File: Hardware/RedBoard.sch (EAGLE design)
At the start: 65 parts, among them IC3 LM1117, J1 POWER_JACKOVERPASTE_REDBOARD_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, J2 ICSP, Q1 ZXMP6A13FTA, Q2 2N7002PW, U1 FT231XS, U2 MIC5205, U3 ATMEGA328, Y1 16MHz

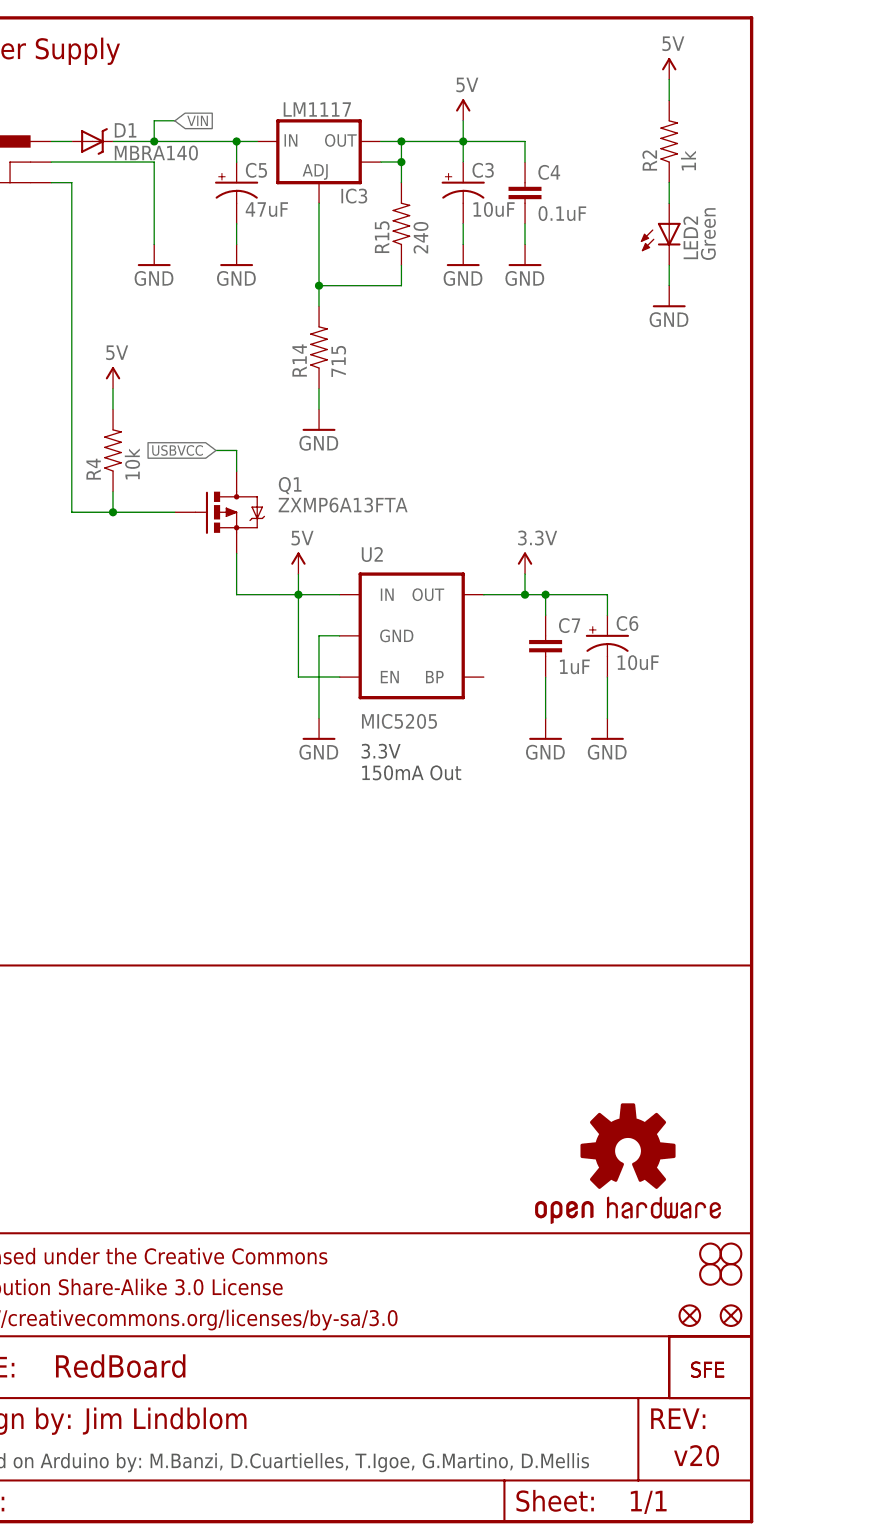
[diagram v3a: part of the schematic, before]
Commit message: Moved C1 cap around silk. Moved some top silk.
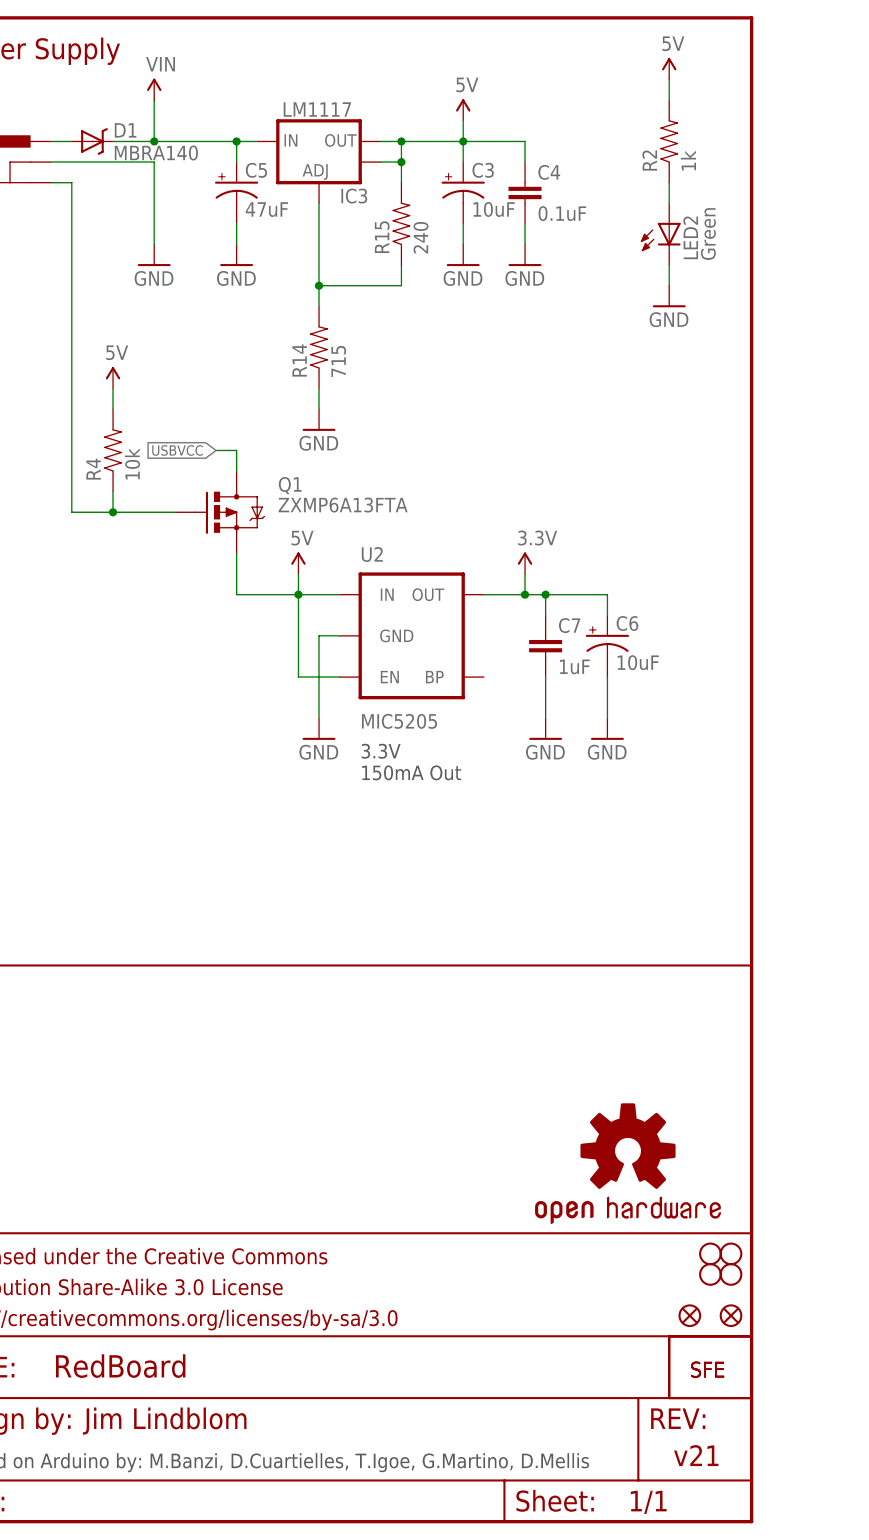
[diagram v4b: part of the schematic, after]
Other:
- note added: "v21"
- note removed: "v20"
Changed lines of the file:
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@@
 <grid distance="0.1" unitdist="inch" unit="inch" style="lines" multiple="1" display="no" altdistance="0.01" altunitdist="inch" altunit="inch"/>
 <layers>
-<layer number="1" name="Top" color="4" fill="1" visible="yes" active="no"/>
-<layer number="2" name="Route2" color="1" fill="3" visible="yes" active="no"/>
-<layer number="3" name="Route3" color="4" fill="3" visible="yes" active="no"/>
-<layer number="4" name="Route4" color="1" fill="4" visible="yes" active="no"/>
-<layer number="5" name="Route5" color="4" fill="4" visible="yes" active="no"/>
-<layer number="6" name="Route6" color="1" fill="8" visible="yes" active="no"/>
-<layer number="7" name="Route7" color="4" fill="8" visible="yes" active="no"/>
-<layer number="8" name="Route8" color="1" fill="2" visible="yes" active="no"/>
-<layer number="9" name="Route9" color="4" fill="2" visible="yes" active="no"/>
-<layer number="10" name="Route10" color="1" fill="7" visible="yes" active="no"/>
-<layer number="11" name="Route11" color="4" fill="7" visible="yes" active="no"/>
-<layer number="12" name="Route12" color="1" fill="5" visible="yes" active="no"/>
-<layer number="13" name="Route13" color="4" fill="5" visible="yes" active="no"/>
-<layer number="14" name="Route14" color="1" fill="6" visible="yes" active="no"/>
-<layer number="15" name="Route15" color="4" fill="6" visible="yes" active="no"/>
-<layer number="16" name="Bottom" color="1" fill="1" visible="yes" active="no"/>
-<layer number="17" name="Pads" color="2" fill="1" visible="yes" active="no"/>
-<layer number="18" name="Vias" color="2" fill="1" visible="yes" active="no"/>
-<layer number="19" name="Unrouted" color="6" fill="1" visible="yes" active="no"/>
-<layer number="20" name="Dimension" color="15" fill="1" visible="yes" active="no"/>
-<layer number="21" name="tPlace" color="16" fill="1" visible="yes" active="no"/>
-<layer number="22" name="bPlace" color="14" fill="1" visible="yes" active="no"/>
-<layer number="23" name="tOrigins" color="15" fill="1" visible="yes" active="no"/>
-<layer number="24" name="bOrigins" color="15" fill="1" visible="yes" active="no"/>
-<layer number="25" name="tNames" color="7" fill="1" visible="yes" active="no"/>
-<layer number="26" name="bNames" color="7" fill="1" visible="yes" active="no"/>
-<layer number="27" name="tValues" color="7" fill="1" visible="yes" active="no"/>
-<layer number="28" name="bValues" color="7" fill="1" visible="yes" active="no"/>
+<layer number="1" name="Top" color="4" fill="1" visible="no" active="no"/>
+<layer number="2" name="Route2" color="1" fill="3" visible="no" active="no"/>
+<layer number="3" name="Route3" color="4" fill="3" visible="no" active="no"/>
+<layer number="4" name="Route4" color="1" fill="4" visible="no" active="no"/>
+<layer number="5" name="Route5" color="4" fill="4" visible="no" active="no"/>
+<layer number="6" name="Route6" color="1" fill="8" visible="no" active="no"/>
+<layer number="7" name="Route7" color="4" fill="8" visible="no" active="no"/>
+<layer number="8" name="Route8" color="1" fill="2" visible="no" active="no"/>
+<layer number="9" name="Route9" color="4" fill="2" visible="no" active="no"/>
+<layer number="10" name="Route10" color="1" fill="7" visible="no" active="no"/>
+<layer number="11" name="Route11" color="4" fill="7" visible="no" active="no"/>
+<layer number="12" name="Route12" color="1" fill="5" visible="no" active="no"/>
+<layer number="13" name="Route13" color="4" fill="5" visible="no" active="no"/>
+<layer number="14" name="Route14" color="1" fill="6" visible="no" active="no"/>
+<layer number="15" name="Route15" color="4" fill="6" visible="no" active="no"/>
+<layer number="16" name="Bottom" color="1" fill="1" visible="no" active="no"/>
+<layer number="17" name="Pads" color="2" fill="1" visible="no" active="no"/>
+<layer number="18" name="Vias" color="2" fill="1" visible="no" active="no"/>
+<layer number="19" name="Unrouted" color="6" fill="1" visible="no" active="no"/>
+<layer number="20" name="Dimension" color="15" fill="1" visible="no" active="no"/>
+<layer number="21" name="tPlace" color="16" fill="1" visible="no" active="no"/>
+<layer number="22" name="bPlace" color="14" fill="1" visible="no" active="no"/>
+<layer number="23" name="tOrigins" color="15" fill="1" visible="no" active="no"/>
+<layer number="24" name="bOrigins" color="15" fill="1" visible="no" active="no"/>
+<layer number="25" name="tNames" color="7" fill="1" visible="no" active="no"/>
+<layer number="26" name="bNames" color="7" fill="1" visible="no" active="no"/>
+<layer number="27" name="tValues" color="7" fill="1" visible="no" active="no"/>
+<layer number="28" name="bValues" color="7" fill="1" visible="no" active="no"/>
 <layer number="29" name="tStop" color="2" fill="3" visible="no" active="no"/>
 <layer number="30" name="bStop" color="5" fill="6" visible="no" active="no"/>
@@
 <layer number="35" name="tGlue" color="7" fill="4" visible="no" active="no"/>
 <layer number="36" name="bGlue" color="7" fill="5" visible="no" active="no"/>
-<layer number="37" name="tTest" color="7" fill="1" visible="yes" active="no"/>
-<layer number="38" name="bTest" color="7" fill="1" visible="yes" active="no"/>
+<layer number="37" name="tTest" color="7" fill="1" visible="no" active="no"/>
+<layer number="38" name="bTest" color="7" fill="1" visible="no" active="no"/>
 <layer number="39" name="tKeepout" color="4" fill="11" visible="no" active="no"/>
 <layer number="40" name="bKeepout" color="1" fill="11" visible="no" active="no"/>
@@
 <layer number="44" name="Drills" color="7" fill="1" visible="no" active="no"/>
 <layer number="45" name="Holes" color="7" fill="1" visible="no" active="no"/>
-<layer number="46" name="Milling" color="3" fill="1" visible="yes" active="no"/>
-<layer number="47" name="Measures" color="7" fill="1" visible="yes" active="no"/>
-<layer number="48" name="Document" color="7" fill="1" visible="yes" active="no"/>
-<layer number="49" name="Reference" color="13" fill="1" visible="yes" active="no"/>
-<layer number="50" name="dxf" color="12" fill="1" visible="yes" active="no"/>
-<layer number="51" name="tDocu" color="6" fill="1" visible="yes" active="no"/>
-<layer number="52" name="bDocu" color="7" fill="1" visible="yes" active="no"/>
-<layer number="53" name="tGND_GNDA" color="7" fill="1" visible="yes" active="no"/>
-<layer number="54" name="bGND_GNDA" color="7" fill="1" visible="yes" active="no"/>
-<layer number="56" name="wert" color="7" fill="1" visible="yes" active="no"/>
+<layer number="46" name="Milling" color="3" fill="1" visible="no" active="no"/>
+<layer number="47" name="Measures" color="7" fill="1" visible="no" active="no"/>
+<layer number="48" name="Document" color="7" fill="1" visible="no" active="no"/>
+<layer number="49" name="Reference" color="13" fill="1" visible="no" active="no"/>
+<layer number="50" name="dxf" color="12" fill="1" visible="no" active="no"/>
+<layer number="51" name="tDocu" color="6" fill="1" visible="no" active="no"/>
+<layer number="52" name="bDocu" color="7" fill="1" visible="no" active="no"/>
+<layer number="53" name="tGND_GNDA" color="7" fill="1" visible="no" active="no"/>
+<layer number="54" name="bGND_GNDA" color="7" fill="1" visible="no" active="no"/>
+<layer number="56" name="wert" color="7" fill="1" visible="no" active="no"/>
 <layer number="91" name="Nets" color="2" fill="1" visible="yes" active="yes"/>
 <layer number="92" name="Busses" color="1" fill="1" visible="yes" active="yes"/>
@@
 <part name="LED3" library="SparkFun-LED" deviceset="LED" device="1206-NS" value="Red"/>
 <part name="J1" library="Testing" deviceset="POWER_JACK" device="OVERPASTE_REDBOARD_0603"/>
+<part name="SUPPLY7" library="SparkFun-Aesthetics" deviceset="VIN" device=""/>
 </parts>
 <sheets>
@@
 <wire x1="147.32" y1="68.58" x2="248.92" y2="68.58" width="0.254" layer="94"/>
 <text x="166.624" y="11.43" size="2.54" layer="94">Jim Lindblom</text>
-<text x="239.268" y="6.858" size="2.54" layer="94">v20</text>
+<text x="239.268" y="6.858" size="2.54" layer="94">v21</text>
 </plain>
 <instances>
@@
 <instance part="LED3" gate="G$1" x="129.54" y="15.24" rot="R270"/>
 <instance part="J1" gate="G$1" x="160.02" y="162.56"/>
+<instance part="SUPPLY7" gate="G$1" x="175.26" y="175.26"/>
 </instances>
 <busses>
@@
 <pinref part="D1" gate="G$1" pin="C"/>
 <wire x1="175.26" y1="170.18" x2="170.18" y2="170.18" width="0.1524" layer="91"/>
-<wire x1="175.26" y1="170.18" x2="175.26" y2="172.72" width="0.1524" layer="91"/>
 <junction x="175.26" y="170.18"/>
-<wire x1="175.26" y1="172.72" x2="177.8" y2="172.72" width="0.1524" layer="91"/>
-<label x="177.8" y="172.72" size="1.27" layer="95" xref="yes"/>
-</segment>
-</net>
+<pinref part="SUPPLY7" gate="G$1" pin="VIN"/>
+<wire x1="175.26" y1="170.18" x2="175.26" y2="175.26" width="0.1524" layer="91"/>
+</segment>
+</net>

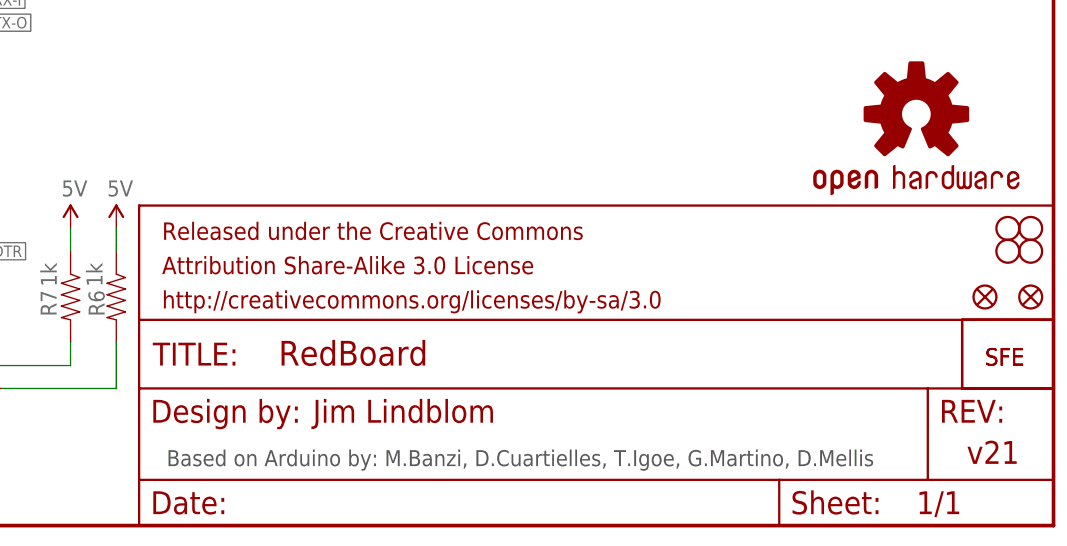
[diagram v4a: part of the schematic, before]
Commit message: Tailing in ISP header pins
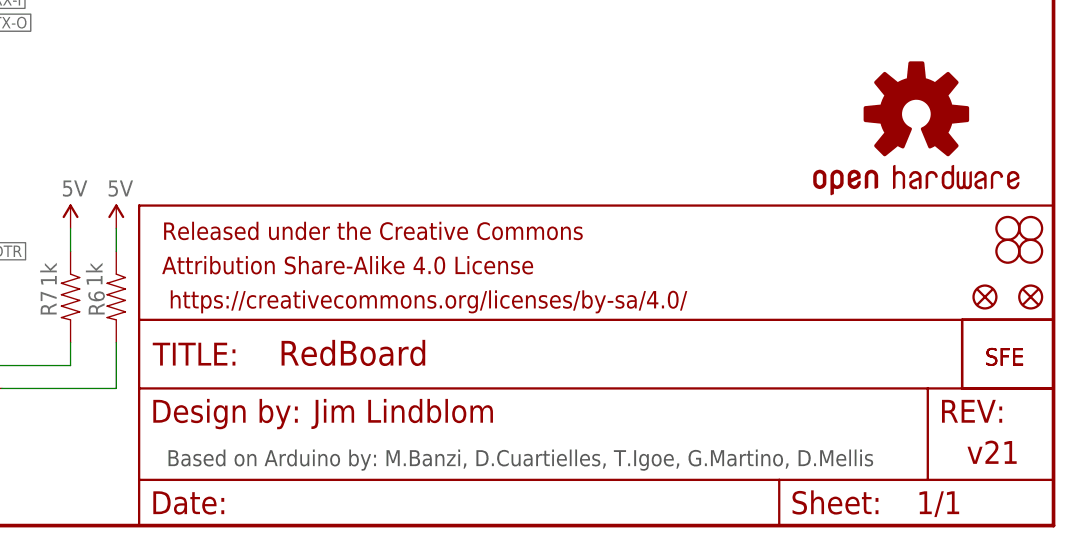
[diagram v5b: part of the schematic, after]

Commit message: Back to old ISP. Tucked in the paste on edge pins
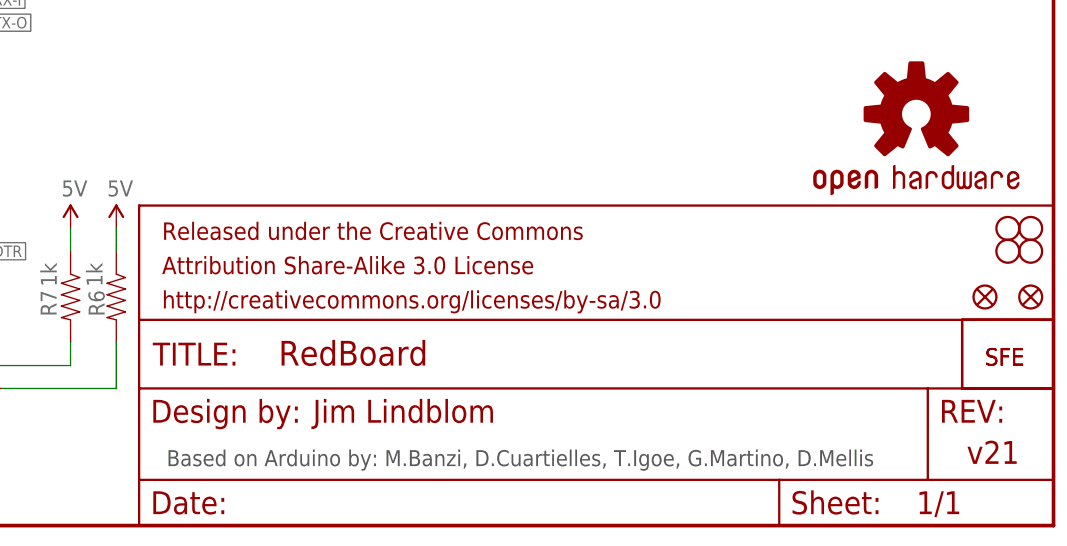
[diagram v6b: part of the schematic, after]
